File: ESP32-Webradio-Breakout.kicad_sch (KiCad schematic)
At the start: 35 parts, among them J1 Conn_01x02, J3 RCJ-042, J4 RCJ-041, Q1 BC547, SW1 RotaryEncoder_Switch, U1 ESP32NodeMCU, U2 TSR_1-2450, U3 PCF8574

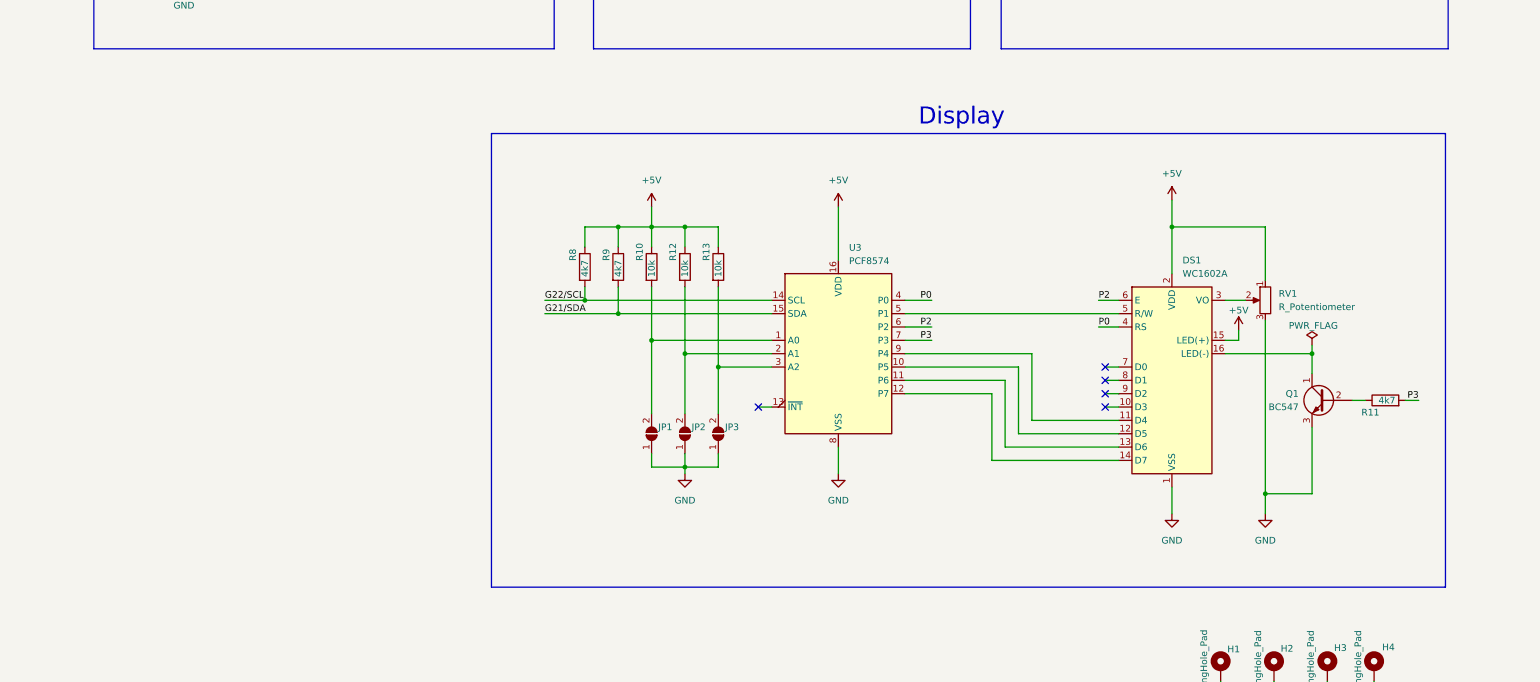
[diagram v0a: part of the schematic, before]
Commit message: Adding Temperatur and Light Sensor. ICs need 100n Cap and DS18B20 connecting to MCU
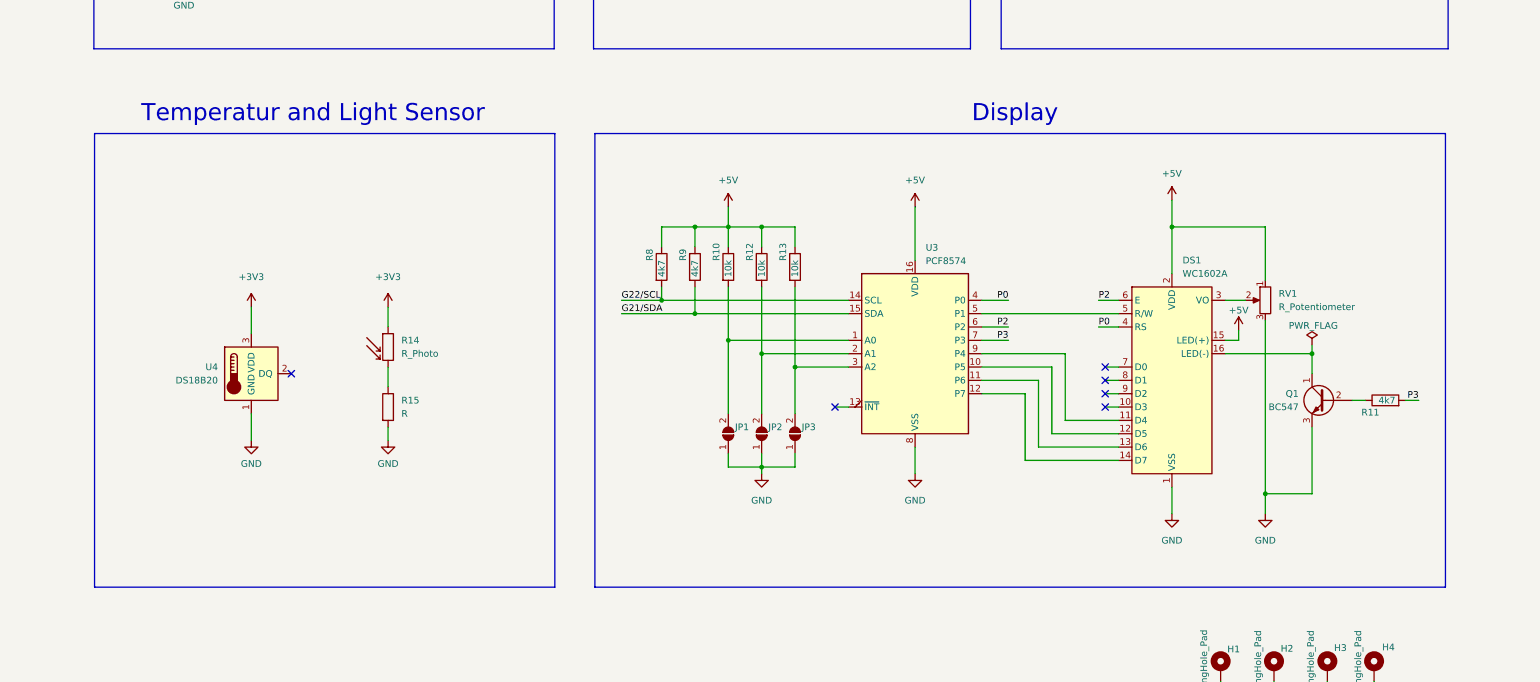
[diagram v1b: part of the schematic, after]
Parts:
- added R14: R_Photo, OptoDevice:R_LDR_5.1x4.3mm_P3.4mm_Vertical, symbol Device:R_Photo
- added R15: R, Resistor_THT:R_Axial_DIN0207_L6.3mm_D2.5mm_P10.16mm_Horizontal, symbol Device:R
- added U4: DS18B20, Package_TO_SOT_THT:TO-92_Inline, symbol Sensor_Temperature:DS18B20
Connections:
- net +3V3: now also R14.1, U4.3 (VDD)
- net GND: now also R15.2, U4.1 (GND)
- new net: R14.2, R15.1
- no-connect marks 22 -> 23
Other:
- note added: "Temperatur and Light Sensor"
- moved on the sheet: JP1, JP2, JP3, R10, R12, R13, R8, R9, U3

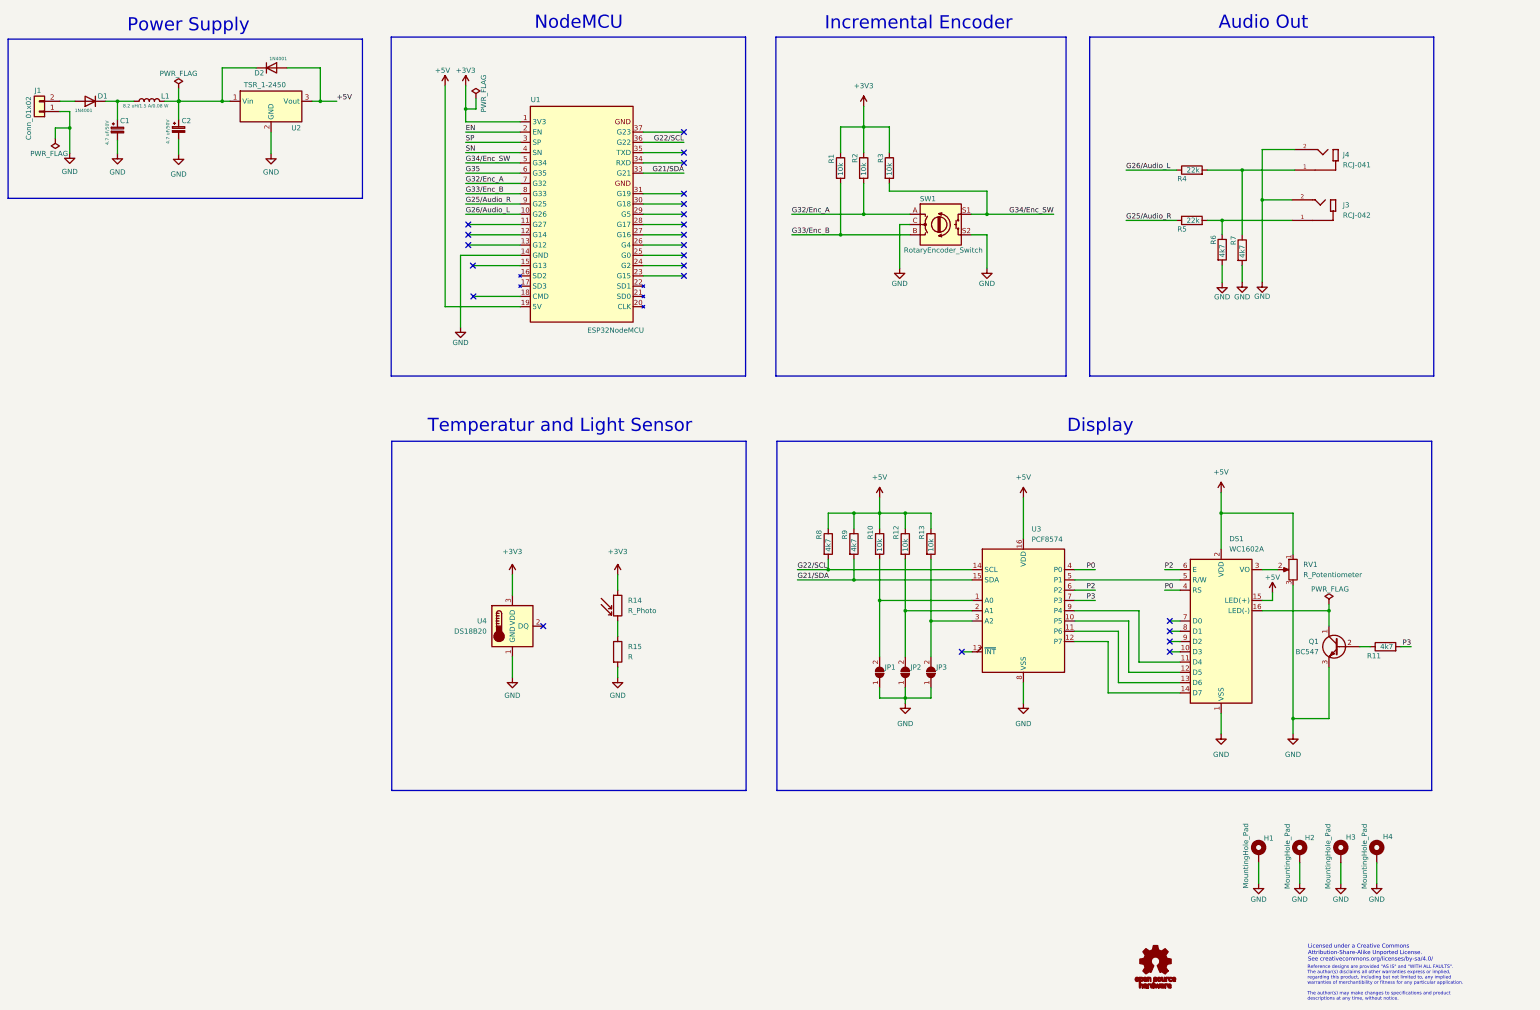
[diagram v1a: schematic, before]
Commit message: Cleanup schematic before adding a new branch.
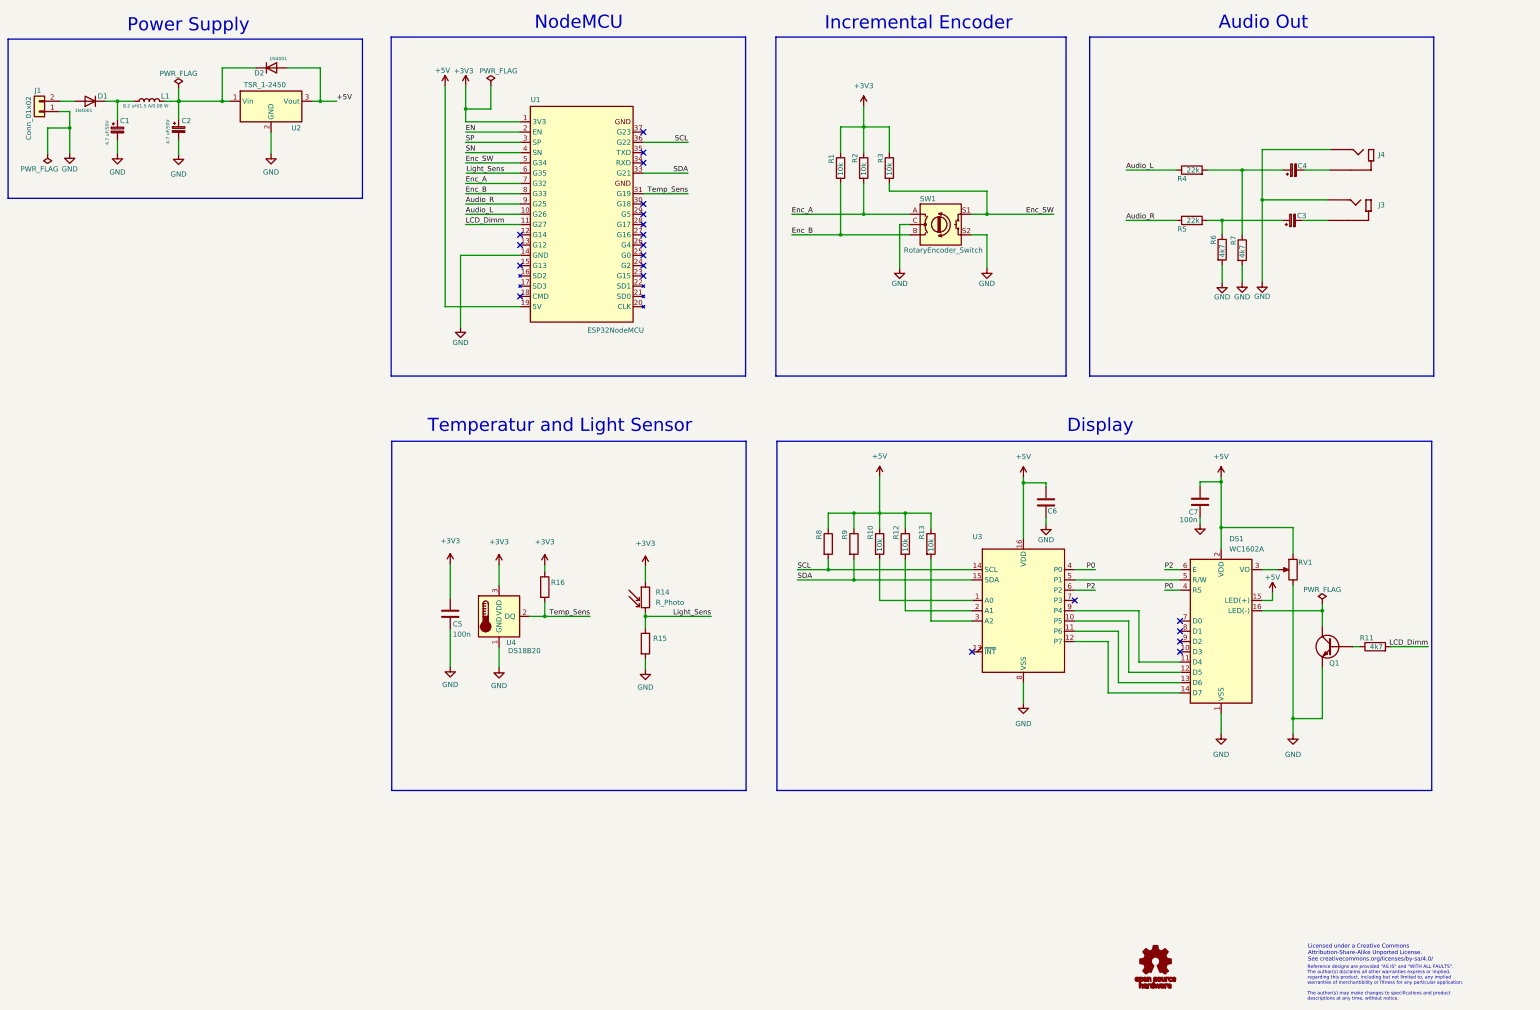
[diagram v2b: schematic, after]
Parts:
- removed H1, H2, H3, H4: MountingHole_Pad, MountingHole:MountingHole_3.2mm_M3_DIN965_Pad, symbol Mechanical:MountingHole_Pad
- removed JP1, JP2, JP3: SolderJumper_2_Open, Jumper:SolderJumper-2_P1.3mm_Open_TrianglePad1.0x1.5mm, symbol Jumper:SolderJumper_2_Open
- added C3, C4: (no value), symbol Device:C_Polarized_Small
- added C5, C7: 100n, symbol Device:C
- added C6: (no value), symbol Device:C
- added R16: (no value), Resistor_THT:R_Axial_DIN0207_L6.3mm_D2.5mm_P10.16mm_Horizontal, symbol Device:R
- J3: value RCJ-042 -> (none); footprint RCJ-042:CUI_RCJ-042 -> (none)
- J4: value RCJ-041 -> (none); footprint RCJ-041:CUI_RCJ-041 -> (none)
- Q1: value BC547 -> (none); footprint Package_TO_SOT_THT:TO-92_Inline -> (none)
- R15: value R -> (none)
- R8, R9: value 4k7 -> (none)
- RV1: value R_Potentiometer -> (none); footprint Potentiometer_THT:Potentiometer_ACP_CA9-V10_Vertical_Hole -> (none)
- U3: value PCF8574 -> (none); footprint Package_DIP:DIP-16_W10.16mm_LongPads -> (none)
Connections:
- net G35 is gone; now on net Light_Sens: U1.6 (G35)
- net +3V3: now also C5.1, R16.1
- net +5V: now also C6.1, C7.1
- net GND: now also C5.2, C6.2, C7.2
- net LCD_Dimm: now reaches U1.11 (G27)
- net LCD_Dimm: now also R11.2
- net Temp_Sens: now reaches U1.31 (G19)
- net Temp_Sens: now also U4.2 (DQ), R16.2
- net Light_Sens: now reaches R14.2, R15.1
- net at R5.2, R6.1: now also C3.1; no longer J3.1
- net at R4.2, R7.1: now also C4.1; no longer J4.1
- net G21/SDA renamed SDA
- net G22/SCL renamed SCL
- net G25/Audio_R renamed Audio_R
- net G26/Audio_L renamed Audio_L
- net G32/Enc_A renamed Enc_A
- net G33/Enc_B renamed Enc_B
- net G34/Enc_SW renamed Enc_SW
- net P3: no longer names the net of U3.7 (P3)
- net P3: no longer R11.2
- new net: C4.2, J4.1
- new net: C3.2, J3.1
- no-connect marks 23 -> 21
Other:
- moved on the sheet: R11, R14, R15, U4
